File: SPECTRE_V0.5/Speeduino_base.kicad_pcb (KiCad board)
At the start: 2 copper layers, 100 x 93 mm, 214 parts, among them J1 Conn_01x04_Male, J2 Conn_02x04_Odd_Even, J3 Conn_01x06_Male, Q1 2N7002, Q10 BSP78, Q11 BSP78, Q12 BSP78, Q13 BSP78, Q14 BSP78, Q15 BSP78, Q16 SMD-MOSFET-N-CH-55V-2.1A-AO34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, Q17 AO3401A, Q18 BSP78, Q19 SMD-MOSFET-N-CH-55V-2.1A-AO34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, Q2 CJ2302, Q20 AO3401A, Q21 SMD-MOSFET-N-CH-55V-2.1A-AO34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, Q22 SMD-MOSFET-N-CH-55V-2.1A-AO34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, Q23 AO3401A, Q24 AO3401A, Q25 BSP78, Q26 BSP78, Q3 CJ2302, Q4 CJ2302, Q5 BSP78, Q6 BSP78, Q7 CJ2302, Q8 CJ2302, Q9 CJ2302, U1 MAX9926UAEE+, U2 molex_48pin, U3 LM78M05_TO220, U4 MAX3232, U5 TL431DBZ

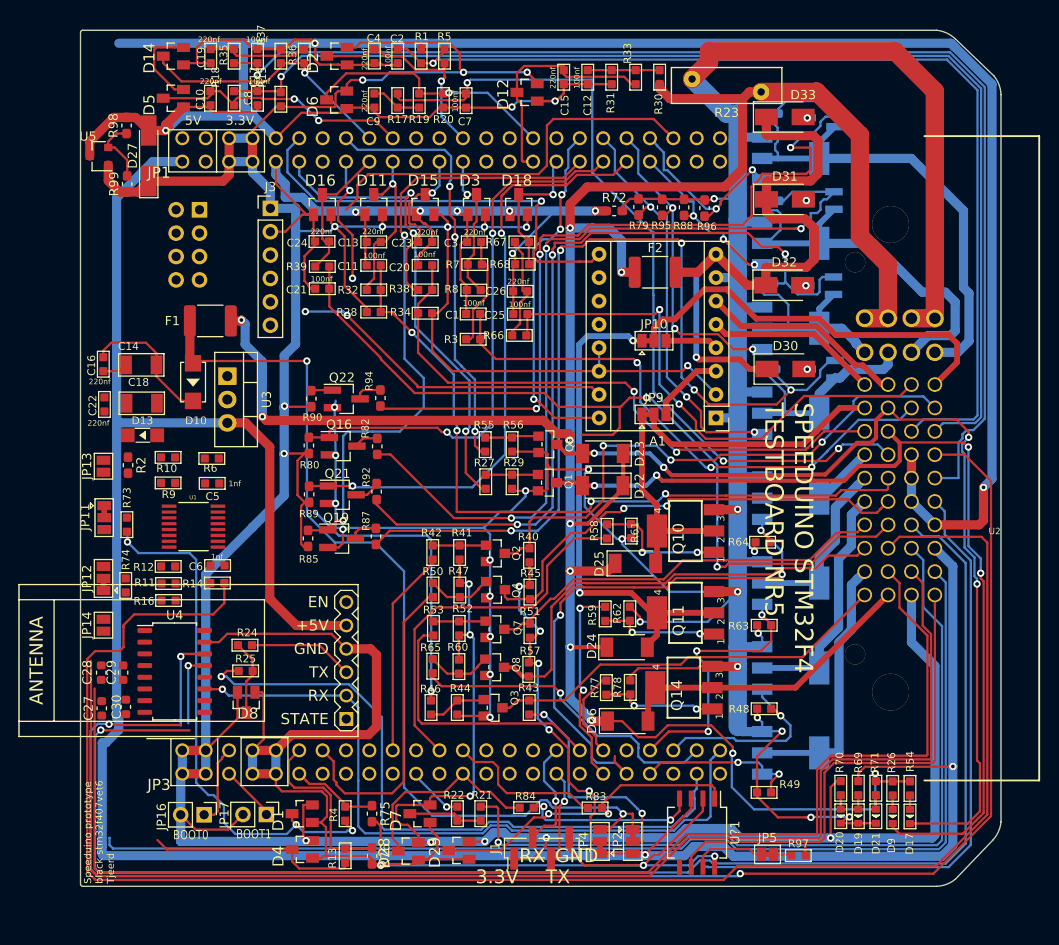
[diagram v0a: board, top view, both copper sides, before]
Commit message: V0.5 fully routed
Routed the whole SPECTRE V0.5 board
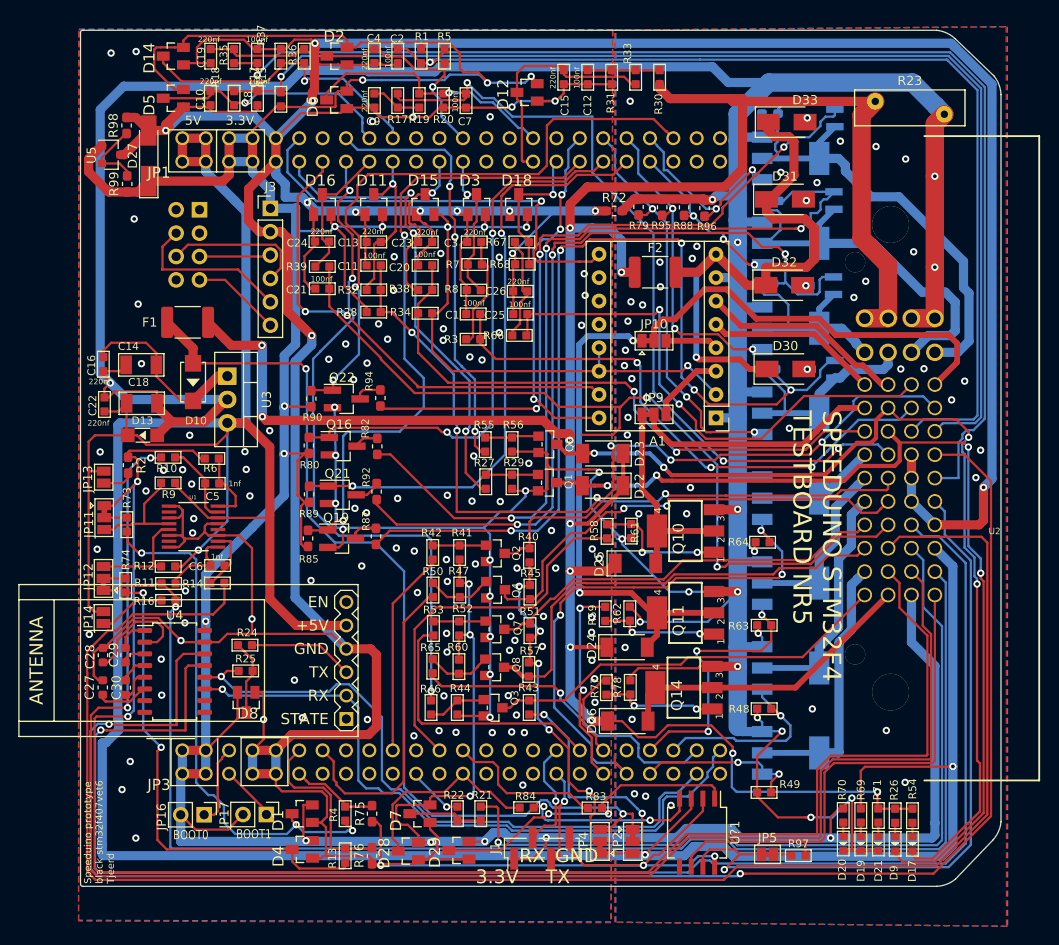
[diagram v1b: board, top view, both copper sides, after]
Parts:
- moved R23 27.7 mm to (207.8, 26.1), turned to 180 degrees
- moved D17 2.98 mm to (204.4, 105.4)
- moved D19 2.98 mm to (198.8, 105.4)
- moved D20 2.98 mm to (196.9, 105.4)
- moved D21 2.98 mm to (200.7, 105.4)
- moved D9 2.98 mm to (202.5, 105.4)
- moved R26 2.98 mm to (202.5, 102.3)
- moved R54 2.98 mm to (204.4, 102.3)
- moved R69 2.98 mm to (198.8, 102.3)
- moved R70 2.98 mm to (196.9, 102.3)
- moved R71 2.98 mm to (200.7, 102.3)
- moved F1 2.47 mm to (125.6, 48.7)
- moved C27 2.27 mm to (116.4, 88.4)
- moved C30 2.10 mm to (118.9, 88.4)
- moved C29 1.92 mm to (118.9, 84.9)
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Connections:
- C10 pad 2: PC2 -> PC0
- D14 pad 3: PC0 -> PC2
- D5 pad 3: PC2 -> PC0
- R18 pad 2: PC2 -> PC0
- R36 pad 1: PC0 -> PC2
- R37 pad 2: PC0 -> PC2
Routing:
- net PWR_GND: track 351.9 -> 486.4 mm, vias 23 -> 67
- net 5V: track 276.6 -> 363.8 mm, vias 2 -> 3
- net GND: track 549.9 -> 631.5 mm, vias 14 -> 113
- net VR1+: track 141.3 -> 185.2 mm, vias 0 -> 2
- net Net-(D4-Pad3): track 23.0 -> 52.7 mm, vias 0 -> 2
- net VR2+: track 122.9 -> 151.6 mm, vias 0 -> 1
- net VR1-: track 144.9 -> 173.3 mm, vias 0 -> 2
- net PC13: track 45.5 -> 73.0 mm
- net 3.3V: track 484.0 -> 509.8 mm, vias 19 -> 20
- net PE15: track 46.3 -> 67.9 mm, vias 0 -> 2
- net BME280_CS: track 0.00 -> 17.8 mm
- net PE5: track 35.8 -> 53.5 mm
- net SPI1_MOSI: track 0.00 -> 15.7 mm
- net Net-(C28-Pad1): track 0.00 -> 12.6 mm
- net Net-(JP11-Pad3): track 0.00 -> 12.5 mm
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- added copper zone on B.Cu, net GND
- added copper zone on F.Cu, net GND
- added copper zone on B.Cu, net PWR_GND
- added copper zone on F.Cu, net PWR_GND

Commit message: Fixed some DRC errors
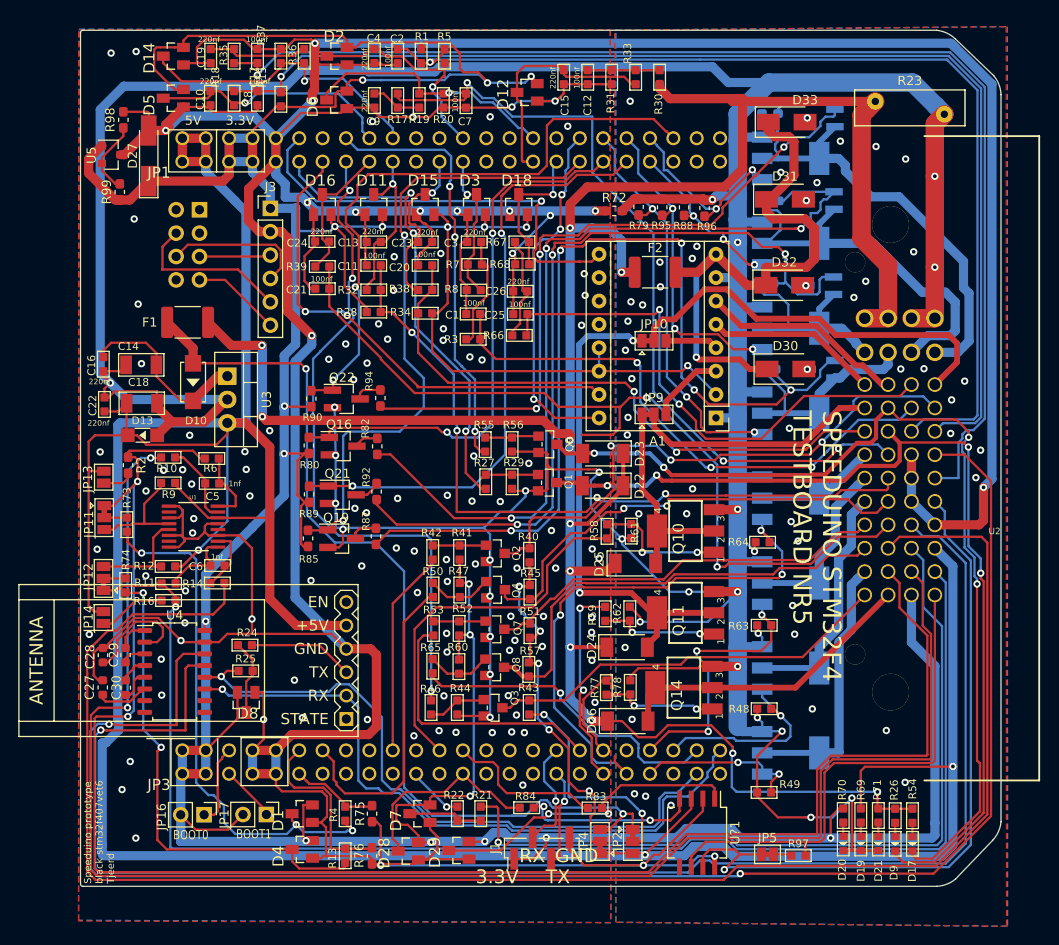
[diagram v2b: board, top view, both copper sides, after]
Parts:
- moved R99 1.19 mm to (118.3, 34.6)
- moved R98 0.70 mm to (118.7, 26.7)
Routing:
- net GND: track 631.5 -> 633.2 mm
- net 3.3V: track 509.8 -> 510.6 mm
- net PWR_GND: vias 67 -> 71

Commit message: Cleanedup acute angles
Cleaned up a lot of the accute angles as suggested by JHolland on the forum
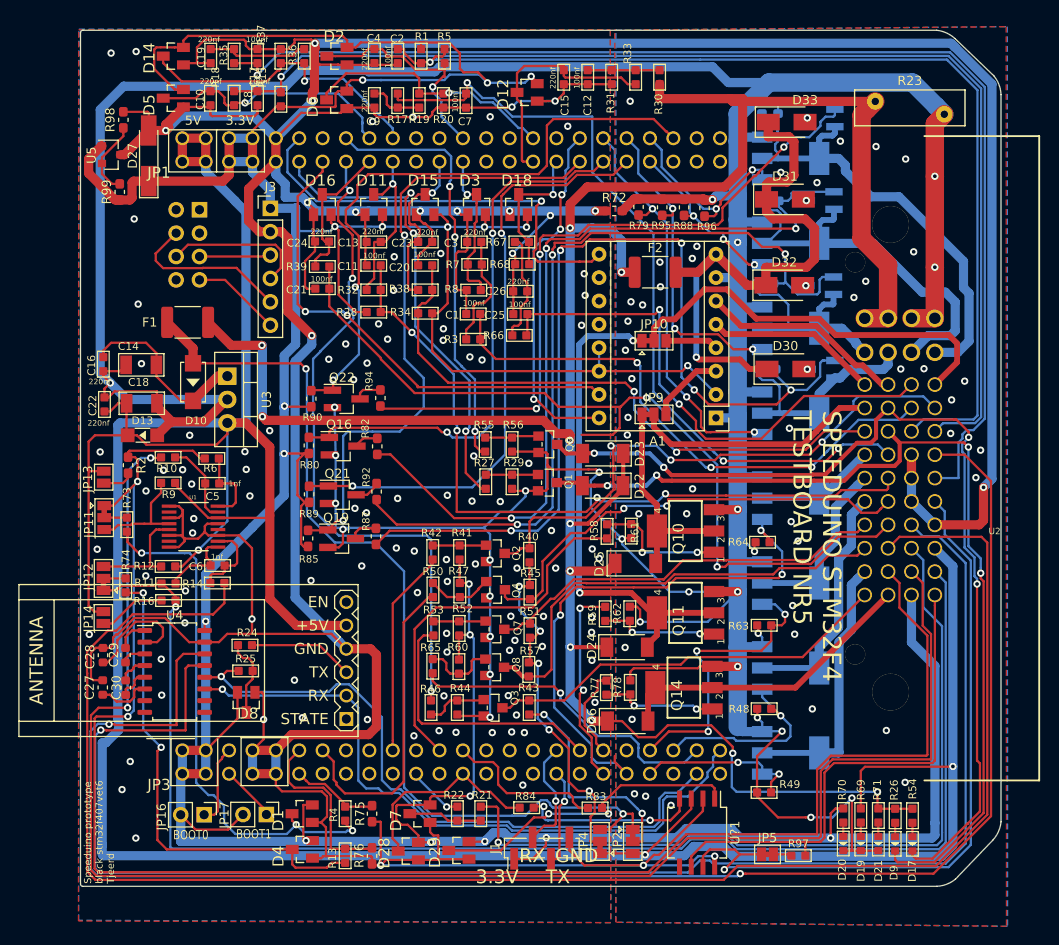
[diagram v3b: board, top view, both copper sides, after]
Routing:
- net GND: track 633.2 -> 637.5 mm, vias 113 -> 112
- net PD14: track 29.5 -> 32.2 mm
- net Net-(Q17-Pad1): track 91.0 -> 88.4 mm
- net 3.3V: track 510.6 -> 513.0 mm
- net INJ8-OUT: track 50.6 -> 53.0 mm
- net V_IDLE: track 62.4 -> 64.1 mm
- net Net-(C6-Pad1): track 7.15 -> 8.84 mm
- net INJ6-OUT: track 23.8 -> 25.1 mm
- net PE13: track 20.5 -> 21.8 mm
- net PWR_GND: track 486.4 -> 487.5 mm
- net Net-(Q20-Pad1): track 101.7 -> 102.7 mm
- net Net-(Q8-Pad1): track 7.06 -> 8.04 mm
- net PE11: track 35.2 -> 36.0 mm
- net INJ5-OUT: track 24.5 -> 25.3 mm
- net PD1: track 17.3 -> 18.1 mm
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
